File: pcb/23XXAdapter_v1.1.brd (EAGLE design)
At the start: 35.6 x 21.6 mm, 29 parts, among them IC1 23XX, IC2 EPROM, IC3 74HCT138N

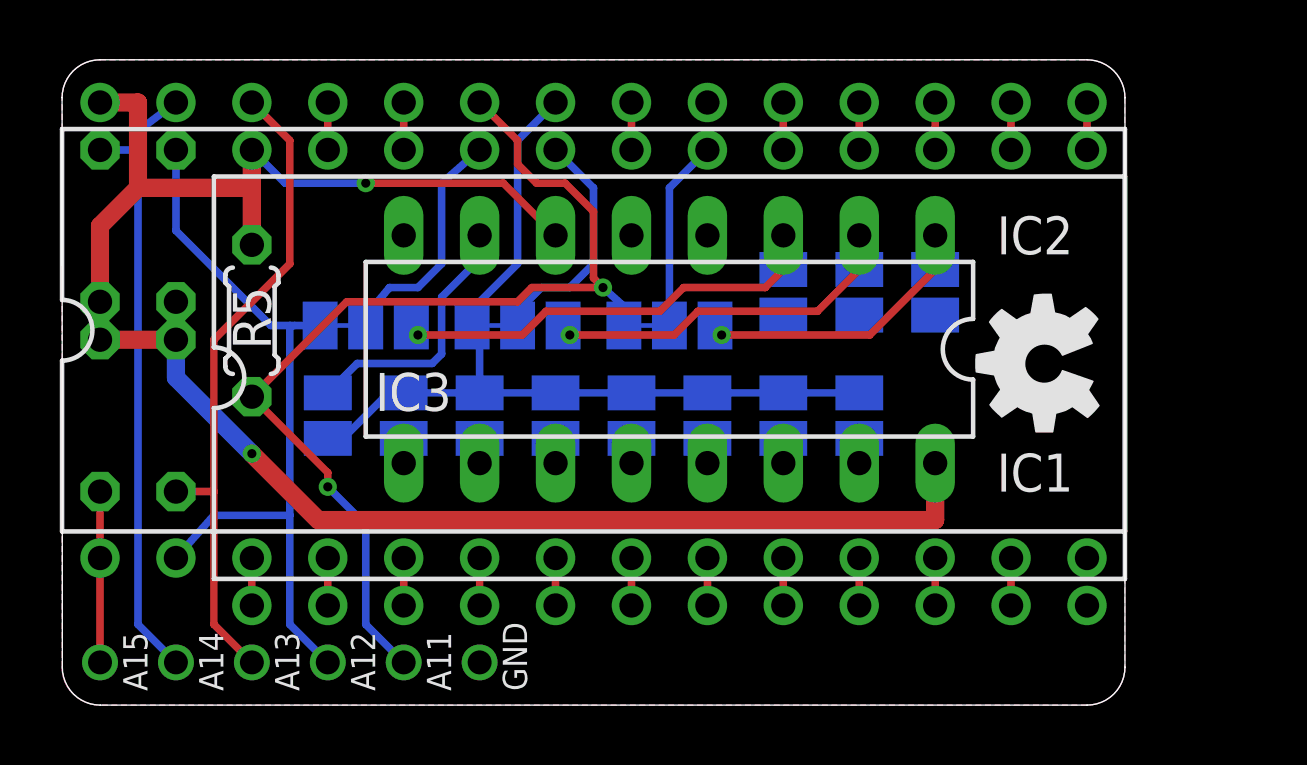
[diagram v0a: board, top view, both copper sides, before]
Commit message: Added BOM and updates to PCB
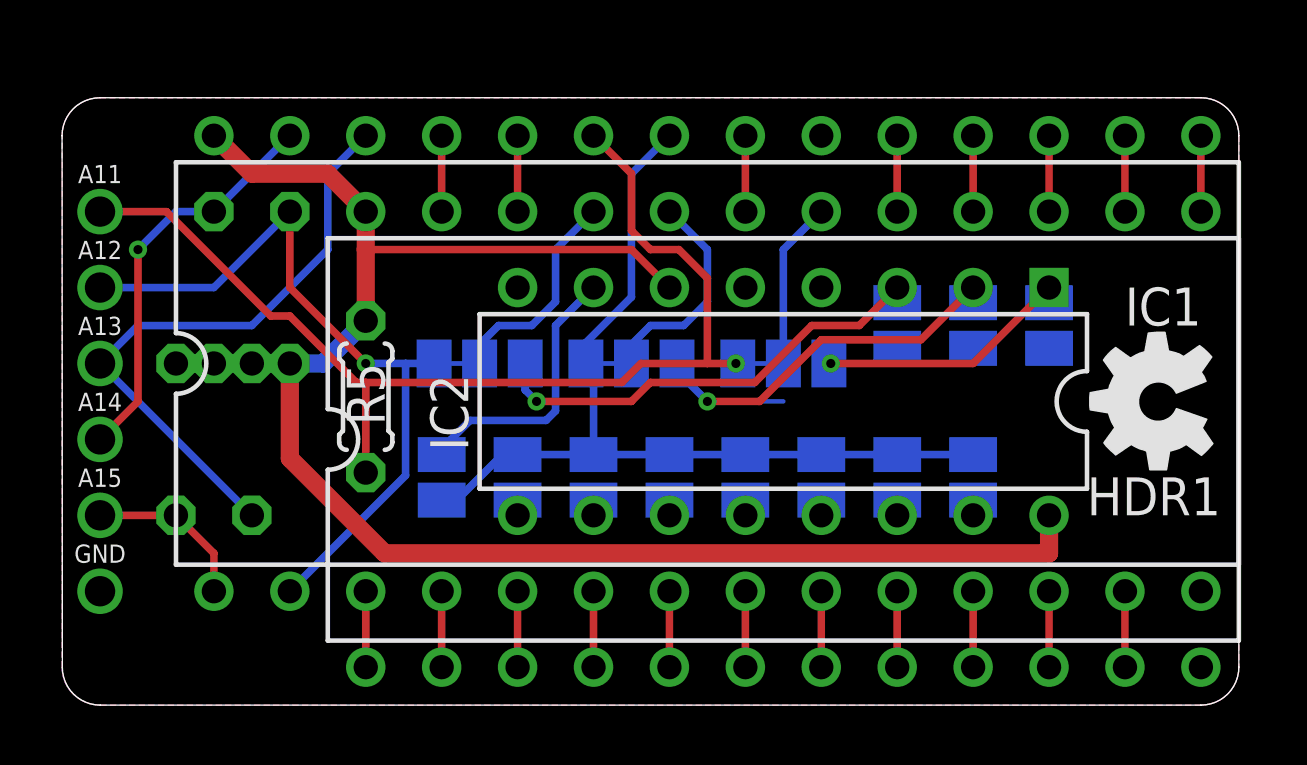
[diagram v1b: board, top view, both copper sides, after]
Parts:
- removed A11, A12, A13, A14, A15, GND: TPTP12R, testpad:TP12R
- removed IC3: 74HCT138N, 74xx-us:DIL16
- added HDR1: 23XX, 0RB_Memory:DIL24-ROUNDPAD
- added X1: (no value), con-lstb-rp:MA06-1
- IC1: value 23XX -> EPROM; device 0RB_Memory:DIL24-ROUNDPAD -> 0RB_Memory:DIL28-ROUNDPAD
- IC2: value EPROM -> 74LS138N; device 0RB_Memory:DIL28-ROUNDPAD -> 74xx-us-jlb:DIL16-RP
- moved IC2 6.78 mm to (24.1, 10.2), turned to 180 degrees
- moved R5 4.58 mm to (10.2, 10.3)
- moved 1 4.33 mm to (27.9, 7.62)
- moved 5 4.33 mm to (17.8, 7.62)
- moved 6 4.33 mm to (15.2, 7.62)
- moved 0 4.33 mm to (30.5, 7.62)
- moved 2 4.33 mm to (25.4, 7.62)
- moved 3 4.33 mm to (22.9, 7.62)
- moved 4 4.33 mm to (20.3, 7.62)
- moved 7 4.33 mm to (12.7, 7.62)
- moved R1 4.33 mm to (7.62, 14.0)
- moved R3 4.33 mm to (5.08, 14.0)
- moved 20 4.02 mm to (19.1, 11.4)
- moved 21 4.02 mm to (14.0, 11.4)
- moved GOLD_ORB_SM1 4.02 mm to (36.7, 10.2)
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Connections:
- net !GCE: now also HDR1.20; no longer IC1.20
- net !OE: now also IC1.22; no longer IC2.22
- net A0: now also HDR1.8, IC1.10; no longer IC1.8, IC2.10
- net A1: now also HDR1.7, IC1.9; no longer IC1.7, IC2.9
- net A10: now also HDR1.19, IC1.21; no longer IC1.19, IC2.21
- net A11: now also IC1.23, X1.6; no longer A11.TP, IC2.23
- net A12: now also IC1.2, X1.5; no longer A12.TP, IC2.2
- net A13: now also IC1.26, X1.4; no longer A13.TP, IC2.26
- net A14: now also IC1.27, X1.3; no longer A14.TP, IC2.27
- net A15: now also IC1.1, X1.2; no longer A15.TP, IC2.1
- net A2: now also HDR1.6, IC1.8; no longer IC1.6, IC2.8
- net A3: now also HDR1.5, IC1.7; no longer IC1.5, IC2.7
- net A4: now also HDR1.4, IC1.6; no longer IC1.4, IC2.6
- net A5: now also HDR1.3, IC1.5; no longer IC1.3, IC2.5
- net A6: now also HDR1.2, IC1.4; no longer IC1.2, IC2.4
- net A7: now also HDR1.1, IC1.3; no longer IC1.1, IC2.3
- net A8: now also HDR1.23, IC1.25; no longer IC1.23, IC2.25
- net A9: now also HDR1.22, IC1.24; no longer IC1.22, IC2.24
- net D0: now also HDR1.9, IC1.11; no longer IC1.9, IC2.11
- net D1: now also HDR1.10, IC1.12; no longer IC1.10, IC2.12
- net D2: now also HDR1.11, IC1.13; no longer IC1.11, IC2.13
- net D3: now also HDR1.13, IC1.15; no longer IC1.13, IC2.15
- net D4: now also HDR1.14, IC1.16; no longer IC1.14, IC2.16
- net D5: now also HDR1.15, IC1.17; no longer IC1.15, IC2.17
- net D6: now also HDR1.16, IC1.18; no longer IC1.16, IC2.18
- net D7: now also HDR1.17, IC1.19; no longer IC1.17, IC2.19
- net GA11: now also HDR1.18; no longer IC1.18
- net GA12: now also HDR1.21; no longer IC1.21
- net GND: now also HDR1.12, IC1.14, IC1.20, IC2.4, IC2.5, IC2.8, X1.1; no longer GND.TP, IC1.12, IC2.14, IC2.20, IC3.4, IC3.5, IC3.8
- net N$1: now also IC2.2; no longer IC3.2
- net N$10: now also IC2.10; no longer IC3.10
- net N$11: now also IC2.9; no longer IC3.9
- net N$12: now also IC2.7; no longer IC3.7
- net N$13: now also IC2.3; no longer IC3.3
- net N$16: now also IC2.1; no longer IC3.1
- net N$4: now also IC2.15; no longer IC3.15
- net N$6: now also IC2.14; no longer IC3.14
- net N$7: now also IC2.13; no longer IC3.13
- net N$8: now also IC2.12; no longer IC3.12
- net N$9: now also IC2.11; no longer IC3.11
- net VCC: now also HDR1.24, IC1.28, IC2.16, IC2.6; no longer IC1.24, IC2.28, IC3.16, IC3.6
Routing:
- net A14: track 21.2 -> 13.5 mm
- net A11: track 34.3 -> 37.2 mm, vias 3 -> 1
- net VCC: track 64.0 -> 61.4 mm, vias 2 -> 0
- net N$16: track 10.7 -> 8.93 mm
- net A13: track 22.1 -> 20.7 mm, vias 1 -> 0
- net N$14: track 0.00 -> 0.95 mm
- net D2: track 1.59 -> 2.54 mm
- net D1: track 1.59 -> 2.54 mm
- net D0: track 1.59 -> 2.54 mm
- net A7: track 1.59 -> 2.54 mm
- net A6: track 1.59 -> 2.54 mm
- net A5: track 1.59 -> 2.54 mm
- net A4: track 1.59 -> 2.54 mm
- net A3: track 1.59 -> 2.54 mm
- net A2: track 1.59 -> 2.54 mm
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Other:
- board size 35.6 x 21.6 mm -> 39.4 x 20.3 mm
- board text added: "A11"
- board text added: "A12"
- board text added: "A13"
- board text added: "A14"
- board text added: "A15"
- board text added: "GND"

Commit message: Update schematic to show VCC/GND and pre-connected pads, h/t Mike Forster
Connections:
- removed net !GCE: 20.2, HDR1.20
- removed net GA11: 18.2, HDR1.18
- removed net GA12: 21.2, HDR1.21
- net !OE: now also 20.2, HDR1.20
- net A11: now also 18.2, HDR1.18
- net A12: now also 21.2, HDR1.21
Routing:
- net A12: track 25.0 -> 33.9 mm
- net !OE: track 30.3 -> 39.2 mm
- net GA12: track 7.31 -> 0.00 mm
- net !GCE: track 7.31 -> 0.00 mm
- net A11: track 37.2 -> 44.4 mm
- net GA11: track 5.61 -> 0.00 mm
- net N$2: track 0.95 -> 0.00 mm
- net N$14: track 0.95 -> 0.00 mm
- net N$3: track 0.63 -> 0.00 mm
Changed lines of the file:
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@@
 </class>
 </classes>
-<designrules name="hackvana *">
+<designrules name="hackvana">
 <description language="de">&lt;b&gt;EAGLE Design Rules für Hackvana&lt;/b&gt;
 &lt;p&gt;
@@
 <param name="dpGapFactor" value="2.5"/>
 <param name="checkGrid" value="0"/>
-<param name="checkAngle" value="1"/>
+<param name="checkAngle" value="0"/>
 <param name="checkFont" value="1"/>
 <param name="checkRestrict" value="0"/>
@@
 <wire x1="21.59" y1="11.4301" x2="19.3676" y2="11.4301" width="0.254" layer="1"/>
 <contactref element="X1" pad="6"/>
+<contactref element="HDR1" pad="18"/>
+<contactref element="18" pad="2"/>
+<wire x1="25.4" y1="16.51" x2="24.13" y2="15.24" width="0.254" layer="16"/>
+<wire x1="24.13" y1="15.24" x2="24.13" y2="11.43" width="0.254" layer="16"/>
+<wire x1="24.13" y1="11.43" x2="22.606" y2="11.43" width="0.1524" layer="16"/>
 </signal>
 <signal name="A12">
@@
 <wire x1="11.4935" y1="7.6835" x2="11.4935" y2="11.43" width="0.254" layer="16"/>
 <contactref element="X1" pad="5"/>
+<contactref element="HDR1" pad="21"/>
+<contactref element="21" pad="2"/>
+<wire x1="16.51" y1="15.24" x2="16.51" y2="13.4939" width="0.254" layer="16"/>
+<wire x1="16.51" y1="13.4939" x2="15.7161" y2="12.7" width="0.254" layer="16"/>
+<wire x1="17.78" y1="16.51" x2="16.51" y2="15.24" width="0.254" layer="16"/>
+<wire x1="15.7161" y1="12.7" x2="14.605" y2="12.7" width="0.254" layer="16"/>
+<wire x1="14.605" y1="12.7" x2="13.97" y2="12.065" width="0.254" layer="16"/>
+<wire x1="13.97" y1="12.065" x2="13.97" y2="11.43" width="0.254" layer="16"/>
+<wire x1="12.446" y1="11.43" x2="13.97" y2="11.43" width="0.1524" layer="16"/>
 </signal>
 <signal name="A13">
@@
 <wire x1="5.08" y1="5.08" x2="3.81" y2="6.35" width="0.254" layer="1"/>
 <contactref element="X1" pad="2"/>
-</signal>
-<signal name="GA12">
-<contactref element="HDR1" pad="21"/>
-<contactref element="21" pad="2"/>
-<wire x1="16.51" y1="15.24" x2="16.51" y2="13.4939" width="0.254" layer="16"/>
-<wire x1="16.51" y1="13.4939" x2="15.7161" y2="12.7" width="0.254" layer="16"/>
-<wire x1="17.78" y1="16.51" x2="16.51" y2="15.24" width="0.254" layer="16"/>
-<wire x1="15.7161" y1="12.7" x2="14.605" y2="12.7" width="0.254" layer="16"/>
-<wire x1="14.605" y1="12.7" x2="13.97" y2="12.065" width="0.254" layer="16"/>
-<wire x1="13.97" y1="12.065" x2="13.97" y2="11.43" width="0.254" layer="16"/>
 </signal>
 <signal name="!OE">
@@
 <wire x1="19.05" y1="13.6525" x2="17.526" y2="12.1285" width="0.254" layer="16"/>
 <wire x1="17.526" y1="12.1285" x2="17.526" y2="11.43" width="0.254" layer="16"/>
+<contactref element="HDR1" pad="20"/>
+<contactref element="20" pad="2"/>
+<wire x1="21.59" y1="13.4939" x2="21.59" y2="15.24" width="0.254" layer="16"/>
+<wire x1="20.7962" y1="12.7001" x2="21.59" y2="13.4939" width="0.254" layer="16"/>
+<wire x1="20.32" y1="16.51" x2="21.59" y2="15.24" width="0.254" layer="16"/>
+<wire x1="20.7962" y1="12.7001" x2="19.6851" y2="12.7001" width="0.254" layer="16"/>
+<wire x1="19.6851" y1="12.7001" x2="19.05" y2="12.065" width="0.254" layer="16"/>
+<wire x1="19.05" y1="12.065" x2="19.05" y2="11.43" width="0.254" layer="16"/>
+<wire x1="19.05" y1="11.43" x2="17.526" y2="11.43" width="0.1524" layer="16"/>
 </signal>
 <signal name="N$4">
@@
 <wire x1="23.1775" y1="10.795" x2="19.685" y2="10.795" width="0.254" layer="1"/>
 </signal>
-<signal name="!GCE">
-<contactref element="HDR1" pad="20"/>
-<contactref element="20" pad="2"/>
-<wire x1="21.59" y1="13.4939" x2="21.59" y2="15.24" width="0.254" layer="16"/>
-<wire x1="20.7962" y1="12.7001" x2="21.59" y2="13.4939" width="0.254" layer="16"/>
-<wire x1="20.32" y1="16.51" x2="21.59" y2="15.24" width="0.254" layer="16"/>
-<wire x1="20.7962" y1="12.7001" x2="19.6851" y2="12.7001" width="0.254" layer="16"/>
-<wire x1="19.6851" y1="12.7001" x2="19.05" y2="12.065" width="0.254" layer="16"/>
-<wire x1="19.05" y1="12.065" x2="19.05" y2="11.43" width="0.254" layer="16"/>
-</signal>
 <signal name="N$1">
 <contactref element="20" pad="3"/>
@@
 <wire x1="23.3362" y1="10.16" x2="21.59" y2="10.16" width="0.254" layer="1"/>
 </signal>
-<signal name="GA11">
-<contactref element="HDR1" pad="18"/>
-<contactref element="18" pad="2"/>
-<wire x1="25.4" y1="16.51" x2="24.13" y2="15.24" width="0.254" layer="16"/>
-<wire x1="24.13" y1="15.24" x2="24.13" y2="11.43" width="0.254" layer="16"/>
-</signal>
 <signal name="N$16">
 <contactref element="18" pad="3"/>
@@
 </signal>
 <signal name="N$2">
-<wire x1="17.78" y1="11.43" x2="18.7325" y2="11.43" width="0.1524" layer="16"/>
+<wire x1="17.78" y1="11.43" x2="18.7325" y2="11.43" width="0" layer="19" extent="1-16"/>
 </signal>
 <signal name="N$3">
-<wire x1="13.0175" y1="11.43" x2="13.6525" y2="11.43" width="0.1524" layer="16"/>
+<wire x1="13.0175" y1="11.43" x2="13.6525" y2="11.43" width="0" layer="19" extent="1-16"/>
 </signal>
 <signal name="N$5">
@@
 </signal>
 <signal name="N$14">
-<wire x1="22.86" y1="11.43" x2="23.8125" y2="11.43" width="0.1524" layer="16"/>
+<wire x1="22.86" y1="11.43" x2="23.8125" y2="11.43" width="0" layer="19" extent="1-16"/>
 </signal>
 </signals>

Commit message: PCB cleanup and additional images
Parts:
- added R1', R2', R3', R4', R5': (no value), resistor:R0805
- moved R5 6.51 mm to (3.81, 8.89), flipped to the bottom
- moved R2 5.24 mm to (7.62, 14.0), turned to 270 degrees
- moved R3 5.24 mm to (6.35, 8.89), turned to 90 degrees
- moved R4 5.24 mm to (5.08, 14.0), turned to 270 degrees
- moved R1 4.45 mm to (10.2, 10.3), flipped to the top, turned to 90 degrees
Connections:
- net A11: now also R1'.1, R1.1; no longer R5.1
- net A12: now also R2'.1, R2.1; no longer R1.1
- net A13: now also R3'.1, R3.1; no longer R2.1
- net A14: now also R4'.1, R4.1; no longer R3.1
- net A15: now also R5'.1, R5.1; no longer R4.1
- net VCC: now also R1'.2, R2'.2, R3'.2, R4'.2, R5'.2
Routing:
- net VCC: track 61.4 -> 70.3 mm
- net A11: track 44.4 -> 49.8 mm
- net A14: track 13.5 -> 15.2 mm
- net A15: track 5.61 -> 7.30 mm
- net A13: track 20.7 -> 22.4 mm, vias 0 -> 1
- net A12: track 33.9 -> 34.7 mm
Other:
- board text added: "(c) 2012-24"
- board text added: "go4retro.com"
- board text removed: "(c) 2012 RETRO Innovations"
- board text removed: "www.go4retro.com"
